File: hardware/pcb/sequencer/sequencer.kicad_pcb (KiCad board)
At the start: 2 copper layers, 81.8 x 129.5 mm, 96 parts, among them J1 Conn_02x08_Odd_Even, J2 Conn_02x08_Odd_Even, SW1 SW_SPST, SW10 SW_SPST, SW11 SW_SPST, SW12 SW_SPST, SW13 SW_SPST, SW14 SW_SPST, SW15 SW_SPST, SW16 SW_SPST, SW17 SW_SPST, SW18 SW_SPST, SW19 SW_SPST, SW2 SW_SPST, SW20 SW_SPST, SW21 SW_SPST, SW22 SW_SPST, SW23 SW_SPST, SW24 SW_SPST, SW3 SW_SPST, SW4 SW_SPST, SW5 SW_SPST, SW6 SW_SPST, SW7 SW_SPST, SW8 SW_SPST, SW9 SW_SPST

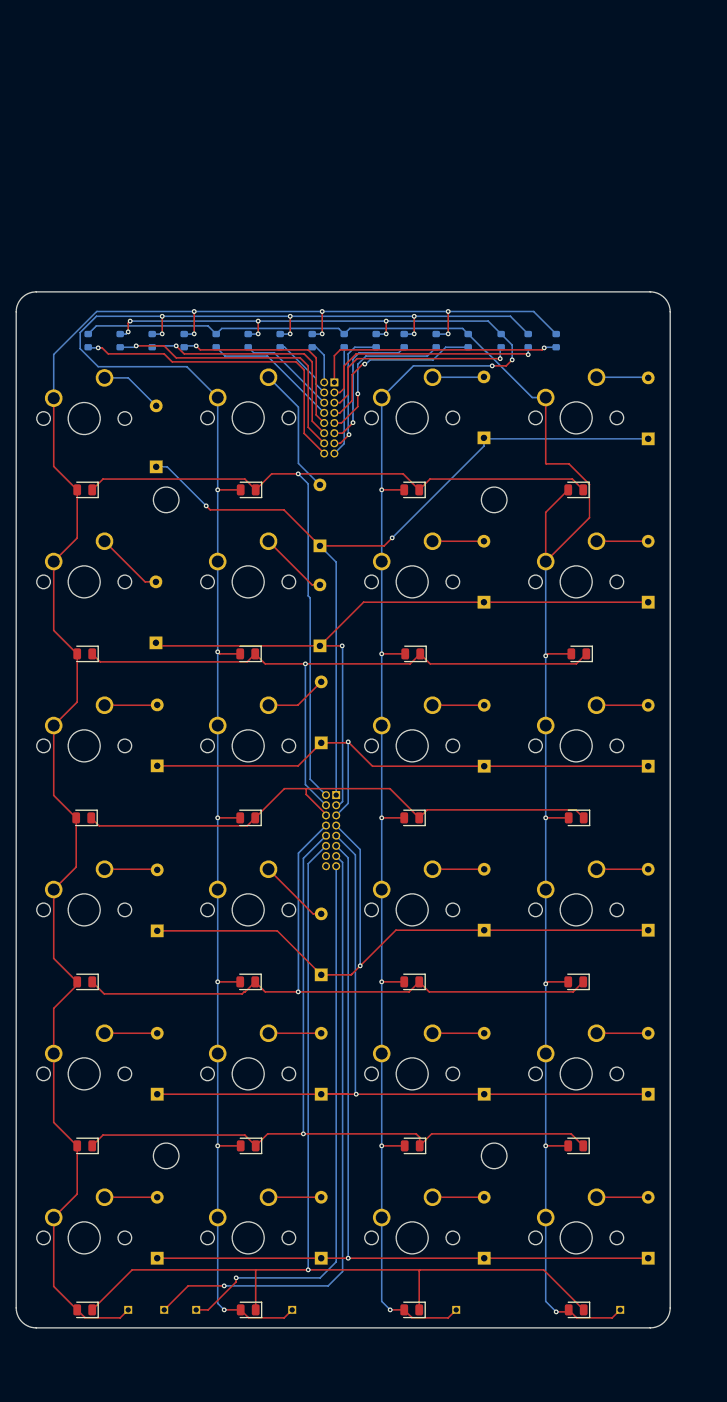
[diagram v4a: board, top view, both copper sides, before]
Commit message: sequencer: move keys and controls to this pcb
it's just easier to do it this way
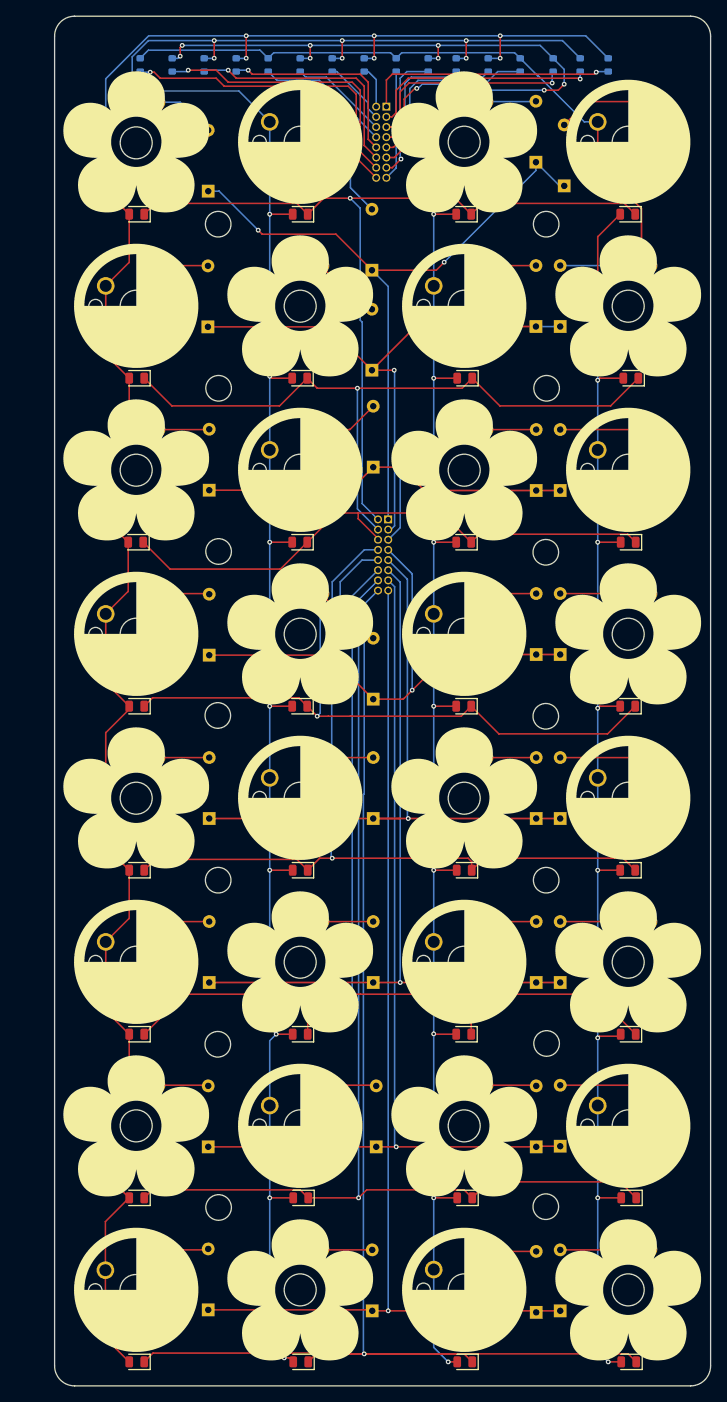
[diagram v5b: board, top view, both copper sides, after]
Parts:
- removed COL (x4), ROW7, ROW8: Conn_01x01, Connector_PinHeader_1.27mm:PinHeader_1x01_P1.27mm_Vertical
- added D49: D, Diode_THT:D_DO-35_SOD27_P7.62mm_Horizontal, B.Cu at (76.5, 159.6)
- added D50: D, Diode_THT:D_DO-35_SOD27_P7.62mm_Horizontal, B.Cu at (97.5, 159.6)
- added D51: D, Diode_THT:D_DO-35_SOD27_P7.62mm_Horizontal, B.Cu at (117.5, 159.6)
- added D52: D, Diode_THT:D_DO-35_SOD27_P7.62mm_Horizontal, B.Cu at (120.5, 159.5)
- added D53: D, Diode_THT:D_DO-35_SOD27_P7.62mm_Horizontal, B.Cu at (76.5, 180.0)
- added D54: D, Diode_THT:D_DO-35_SOD27_P7.62mm_Horizontal, B.Cu at (97.0, 180.1)
- added D55: D, Diode_THT:D_DO-35_SOD27_P7.62mm_Horizontal, B.Cu at (117.5, 180.3)
- added D56: D, Diode_THT:D_DO-35_SOD27_P7.62mm_Horizontal, B.Cu at (120.5, 180.1)
- added D57: LED, LED_SMD:LED_0805_2012Metric, F.Cu at (67.6, 166.0)
- added D58: LED, LED_SMD:LED_0805_2012Metric, F.Cu at (88.1, 166.0)
- added D59: LED, LED_SMD:LED_0805_2012Metric, F.Cu at (108.6, 166.0)
- added D60: LED, LED_SMD:LED_0805_2012Metric, F.Cu at (129.1, 166.0)
- added D61: LED, LED_SMD:LED_0805_2012Metric, F.Cu at (67.6, 186.5)
- added D62: LED, LED_SMD:LED_0805_2012Metric, F.Cu at (88.1, 186.5)
- added D63: LED, LED_SMD:LED_0805_2012Metric, F.Cu at (108.6, 186.5)
- added D64: LED, LED_SMD:LED_0805_2012Metric, F.Cu at (129.1, 186.5)
- added G***: LOGO, sequencer:circle, F.Cu at (67.5, 136.5)
- added G***: LOGO, sequencer:circle, F.Cu at (108.5, 95.5)
- added G***: LOGO, sequencer:flower, F.Cu at (67.5, 116.0)
- added G***: LOGO, sequencer:flower, F.Cu at (88.0, 136.5)
- added G***: LOGO, sequencer:flower, F.Cu at (129.0, 54.5)
- added G***: LOGO, sequencer:circle, F.Cu at (67.5, 177.5)
- added G***: LOGO, sequencer:circle, F.Cu at (67.5, 54.5)
- added G***: LOGO, sequencer:circle, F.Cu at (129.0, 34.0)
- added G***: LOGO, sequencer:circle, F.Cu at (129.0, 75.0)
- added G***: LOGO, sequencer:flower, F.Cu at (88.0, 95.5)
- added G***: LOGO, sequencer:circle, F.Cu at (129.0, 157.0)
- added G***: LOGO, sequencer:flower, F.Cu at (108.5, 116.0)
- added G***: LOGO, sequencer:circle, F.Cu at (88.0, 75.0)
- added G***: LOGO, sequencer:flower, F.Cu at (88.0, 54.5)
- added G***: LOGO, sequencer:circle, F.Cu at (108.5, 54.5)
- added G***: LOGO, sequencer:flower, F.Cu at (129.0, 136.5)
- added G***: LOGO, sequencer:flower, F.Cu at (108.5, 157.0)
- added G***: LOGO, sequencer:flower, F.Cu at (67.5, 34.0)
- added G***: LOGO, sequencer:circle, F.Cu at (108.5, 177.5)
- added G***: LOGO, sequencer:circle, F.Cu at (88.0, 157.0)
- added G***: LOGO, sequencer:circle, F.Cu at (88.0, 116.0)
- added G***: LOGO, sequencer:circle, F.Cu at (67.5, 95.5)
- added G***: LOGO, sequencer:flower, F.Cu at (129.0, 95.5)
- added G***: LOGO, sequencer:flower, F.Cu at (88.0, 177.5)
- added G***: LOGO, sequencer:circle, F.Cu at (88.0, 34.0)
- added G***: LOGO, sequencer:flower, F.Cu at (67.5, 75.0)
- added G***: LOGO, sequencer:circle, F.Cu at (129.0, 116.0)
- added G***: LOGO, sequencer:circle, F.Cu at (108.5, 136.5)
- added G***: LOGO, sequencer:flower, F.Cu at (108.5, 34.0)
- added G***: LOGO, sequencer:flower, F.Cu at (108.5, 75.0)
- added G***: LOGO, sequencer:flower, F.Cu at (129.0, 177.5)
- added G***: LOGO, sequencer:flower, F.Cu at (67.5, 157.0)
- added SW25: SW_SPST, Button_Switch_Keyboard:SW_Cherry_MX_1.00u_PCB, F.Cu at (70.0, 151.9)
- added SW26: SW_SPST, Button_Switch_Keyboard:SW_Cherry_MX_1.00u_PCB, F.Cu at (90.5, 151.9)
- added SW27: SW_SPST, Button_Switch_Keyboard:SW_Cherry_MX_1.00u_PCB, F.Cu at (111.0, 151.9)
- added SW28: SW_SPST, Button_Switch_Keyboard:SW_Cherry_MX_1.00u_PCB, F.Cu at (131.5, 151.9)
- added SW29: SW_SPST, Button_Switch_Keyboard:SW_Cherry_MX_1.00u_PCB, F.Cu at (70.0, 172.5)
- added SW30: SW_SPST, Button_Switch_Keyboard:SW_Cherry_MX_1.00u_PCB, F.Cu at (90.5, 172.4)
- added SW31: SW_SPST, Button_Switch_Keyboard:SW_Cherry_MX_1.00u_PCB, F.Cu at (111.0, 172.4)
- added SW32: SW_SPST, Button_Switch_Keyboard:SW_Cherry_MX_1.00u_PCB, F.Cu at (131.5, 172.4)
- moved D2 40.0 mm to (76.5, 57.1)
- moved D20 36.2 mm to (120.5, 57.1)
- moved D21 36.2 mm to (120.5, 77.6)
- moved D22 36.2 mm to (120.5, 98.1)
- moved D23 36.2 mm to (120.5, 118.6)
- moved D24 36.2 mm to (120.5, 139.1)
- moved D1 35.1 mm to (76.5, 40.2)
- moved D10 35.1 mm to (97.1, 103.7)
- moved D14 35.1 mm to (117.5, 57.1)
- moved D15 35.1 mm to (117.5, 77.6)
- moved D30 35.1 mm to (67.6, 145.5)
- moved D36 35.1 mm to (88.0, 145.5)
- moved D4 35.1 mm to (76.6, 98.2)
- moved D42 35.1 mm to (108.4, 145.5)
- moved D48 35.1 mm to (129.0, 145.5)
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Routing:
- net O16: track 0.00 -> 180.0 mm, vias 0 -> 1
- net O15: track 0.00 -> 143.0 mm, vias 0 -> 1
- net O8: track 69.7 -> 134.2 mm
- net C4: track 214.1 -> 253.5 mm, vias 5 -> 7
- net C3: track 215.2 -> 254.3 mm, vias 14 -> 16
- net O7: track 76.6 -> 115.3 mm
- net C1: track 218.2 -> 256.8 mm
- net C2: track 227.9 -> 266.4 mm, vias 12 -> 14
- net O4: track 84.7 -> 67.2 mm
- net O3: track 73.7 -> 56.2 mm
- net O6: track 113.5 -> 96.0 mm
- net O5: track 98.0 -> 80.5 mm
- net O1: track 103.7 -> 88.0 mm
- net O2: track 86.3 -> 71.5 mm
- net Net-(D56-A): track 0.00 -> 11.2 mm
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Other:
- board size 81.8 x 129.5 mm -> 82 x 171.2 mm

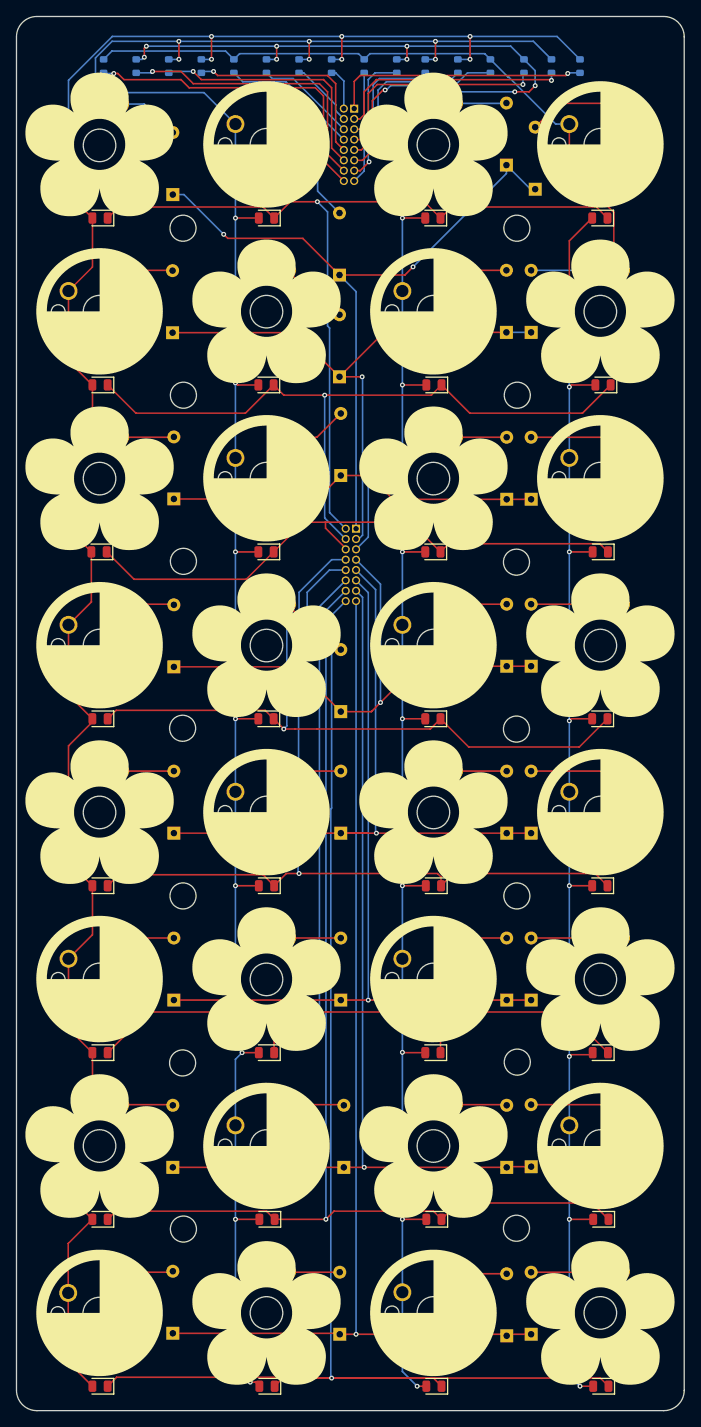
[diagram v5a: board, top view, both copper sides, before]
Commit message: sequencer: move keys closer together
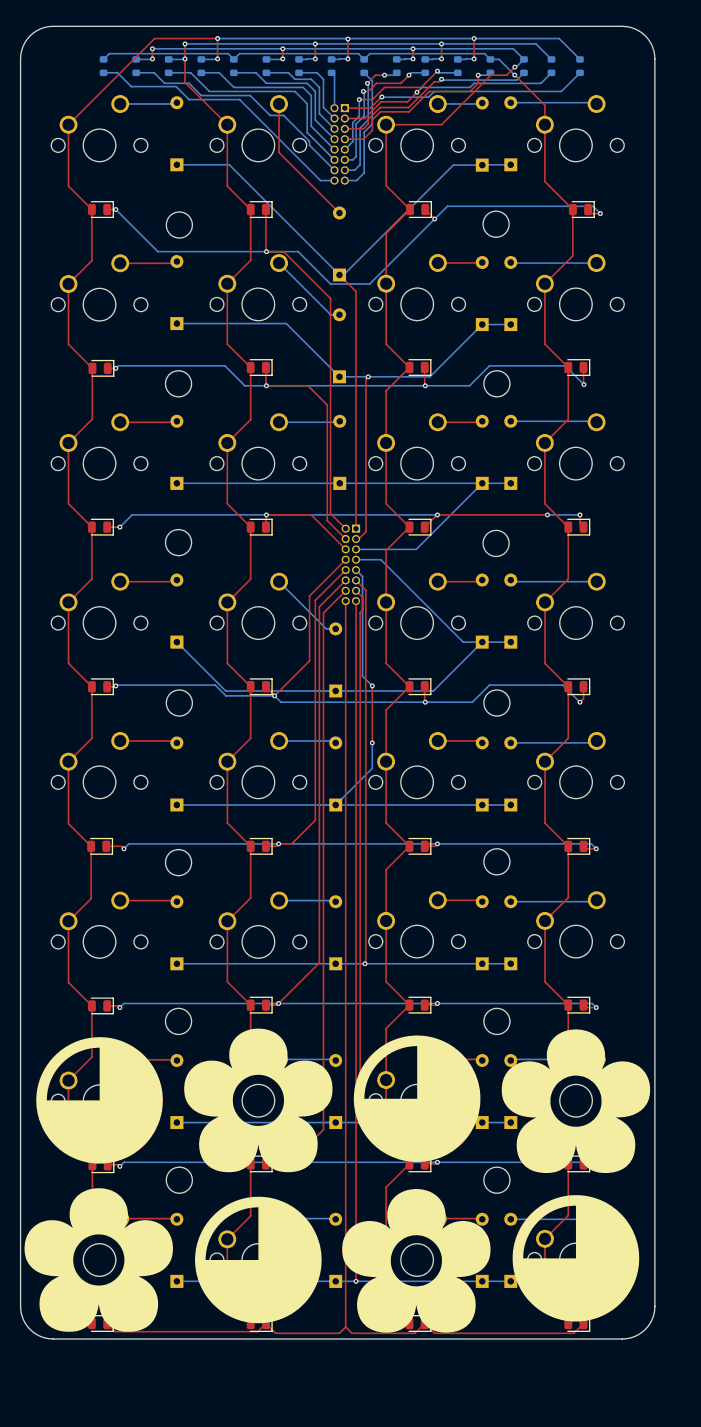
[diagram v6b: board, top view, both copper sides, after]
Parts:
- removed the G*** at (67.5, 136.5)
- removed the G*** at (108.5, 95.5)
- removed the G*** at (67.5, 116.0)
- removed the G*** at (88.0, 136.5)
- removed the G*** at (129.0, 54.5)
- removed the G*** at (67.5, 177.5)
- removed the G*** at (67.5, 54.5)
- removed the G*** at (129.0, 34.0)
- removed the G*** at (129.0, 75.0)
- removed the G*** at (88.0, 95.5)
- removed the G*** at (129.0, 157.0)
- removed the G*** at (108.5, 116.0)
- removed the G*** at (88.0, 75.0)
- removed the G*** at (88.0, 54.5)
- removed the G*** at (108.5, 54.5)
- removed the G*** at (129.0, 136.5)
- removed the G*** at (108.5, 157.0)
- removed the G*** at (67.5, 34.0)
- removed the G*** at (108.5, 177.5)
- removed the G*** at (88.0, 157.0)
- removed the G*** at (88.0, 116.0)
- removed the G*** at (67.5, 95.5)
- removed the G*** at (129.0, 95.5)
- removed the G*** at (88.0, 177.5)
- removed the G*** at (88.0, 34.0)
- removed the G*** at (67.5, 75.0)
- removed the G*** at (129.0, 116.0)
- removed the G*** at (108.5, 136.5)
- removed the G*** at (108.5, 34.0)
- removed the G*** at (108.5, 75.0)
- removed the G*** at (129.0, 177.5)
- removed the G*** at (67.5, 157.0)
- added G***: LOGO, sequencer:circle, F.Cu at (67.5, 151.4)
- added G***: LOGO, sequencer:flower, F.Cu at (106.4, 171.1)
- added G***: LOGO, sequencer:flower, F.Cu at (67.4, 171.0)
- added G***: LOGO, sequencer:flower, F.Cu at (87.0, 151.4)
- added G***: LOGO, sequencer:circle, F.Cu at (87.0, 171.0)
- added G***: LOGO, sequencer:flower, F.Cu at (126.0, 151.5)
- added G***: LOGO, sequencer:circle, F.Cu at (126.0, 170.8)
- added G***: LOGO, sequencer:circle, F.Cu at (106.5, 151.2)
- moved D64 8.29 mm to (126.0, 178.8)
- moved D63 7.97 mm to (106.5, 178.8)
- moved D62 7.77 mm to (87.0, 178.8)
- moved D61 7.70 mm to (67.5, 178.8)
- moved D60 7.46 mm to (126.0, 159.2)
- moved D55 7.33 mm to (114.5, 173.6)
- moved SW32 7.21 mm to (128.6, 165.9)
- moved D59 7.11 mm to (106.5, 159.2)
- moved D56 6.96 mm to (118.0, 173.6)
- moved D58 6.88 mm to (87.0, 159.2)
- moved SW31 6.80 mm to (109.0, 165.9)
- moved D57 6.70 mm to (67.6, 159.3)
- moved SW29 6.58 mm to (70.0, 165.9)
- moved SW30 6.58 mm to (89.5, 165.9)
- moved D48 6.57 mm to (126.0, 139.7)
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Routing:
- net C2: track 266.4 -> 232.6 mm, vias 14 -> 6
- net O16: track 180.0 -> 151.1 mm, vias 1 -> 0
- net C4: track 253.5 -> 226.1 mm, vias 7 -> 1
- net C3: track 254.3 -> 241.3 mm, vias 16 -> 7
- net C1: track 256.8 -> 246.9 mm
- net O8: track 134.2 -> 124.5 mm
- net O9: track 106.9 -> 116.5 mm, vias 1 -> 4
- net O14: track 130.0 -> 120.9 mm, vias 1 -> 4
- net O7: track 115.3 -> 106.8 mm
- net O5: track 80.5 -> 72.5 mm, vias 1 -> 2
- net O6: track 96.0 -> 88.6 mm
- net O10: track 87.3 -> 94.1 mm, vias 1 -> 4
- net I16: track 39.7 -> 33.8 mm, vias 1 -> 0
- net I15: track 35.1 -> 29.6 mm, vias 1 -> 0
- net O12: track 91.1 -> 86.7 mm, vias 1 -> 4
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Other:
- board size 82 x 171.2 mm -> 77.9 x 161.2 mm

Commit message: pcb: version 1 for all boards
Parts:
- J1, J2: footprint Connector_PinHeader_1.27mm:PinHeader_2x08_P1.27mm_Vertical -> Connector_PinHeader_2.54mm:PinHeader_2x08_P2.54mm_Vertical
- moved D7 20.8 mm to (79.0, 39.6)
- moved D8 19.1 mm to (79.0, 56.1)
- moved D9 18.0 mm to (79.0, 75.3)
- moved J2 16.9 mm to (98.0, 64.4)
- moved J1 5.57 mm to (98.0, 35.1)
- moved D1 3.41 mm to (75.5, 39.6)
- moved D3 1.53 mm to (75.5, 75.3)
- moved D2 1.50 mm to (75.5, 56.1)
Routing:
- net O9: track 116.5 -> 91.9 mm, vias 4 -> 5
- net O10: track 94.1 -> 76.8 mm
- net I7: track 16.7 -> 31.3 mm
- net I8: track 15.9 -> 29.5 mm
- net I16: track 33.8 -> 47.3 mm
- net O2: track 67.1 -> 53.8 mm
- net O4: track 65.7 -> 77.3 mm
- net I15: track 29.6 -> 41.1 mm
- net O3: track 59.9 -> 48.4 mm
- net O12: track 86.7 -> 98.1 mm
- net O13: track 103.8 -> 115.1 mm
- net O6: track 88.6 -> 99.6 mm
- net O1: track 84.2 -> 73.4 mm, vias 0 -> 1
- net I6: track 18.5 -> 29.0 mm
- net O14: track 120.9 -> 131.0 mm
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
